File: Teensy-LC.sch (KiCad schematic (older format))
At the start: 37 parts, among them J202 Conn_01x03_Female, J203 I2C_BUS, Q201 SSM3K329R, Q202 SSM3K329R, Q203 SSM3J334R, SW201 SW_Up, SW202 SW_Down, SW203 SW_Enter, U201 LCD 2004A, U202 Teensy-LC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

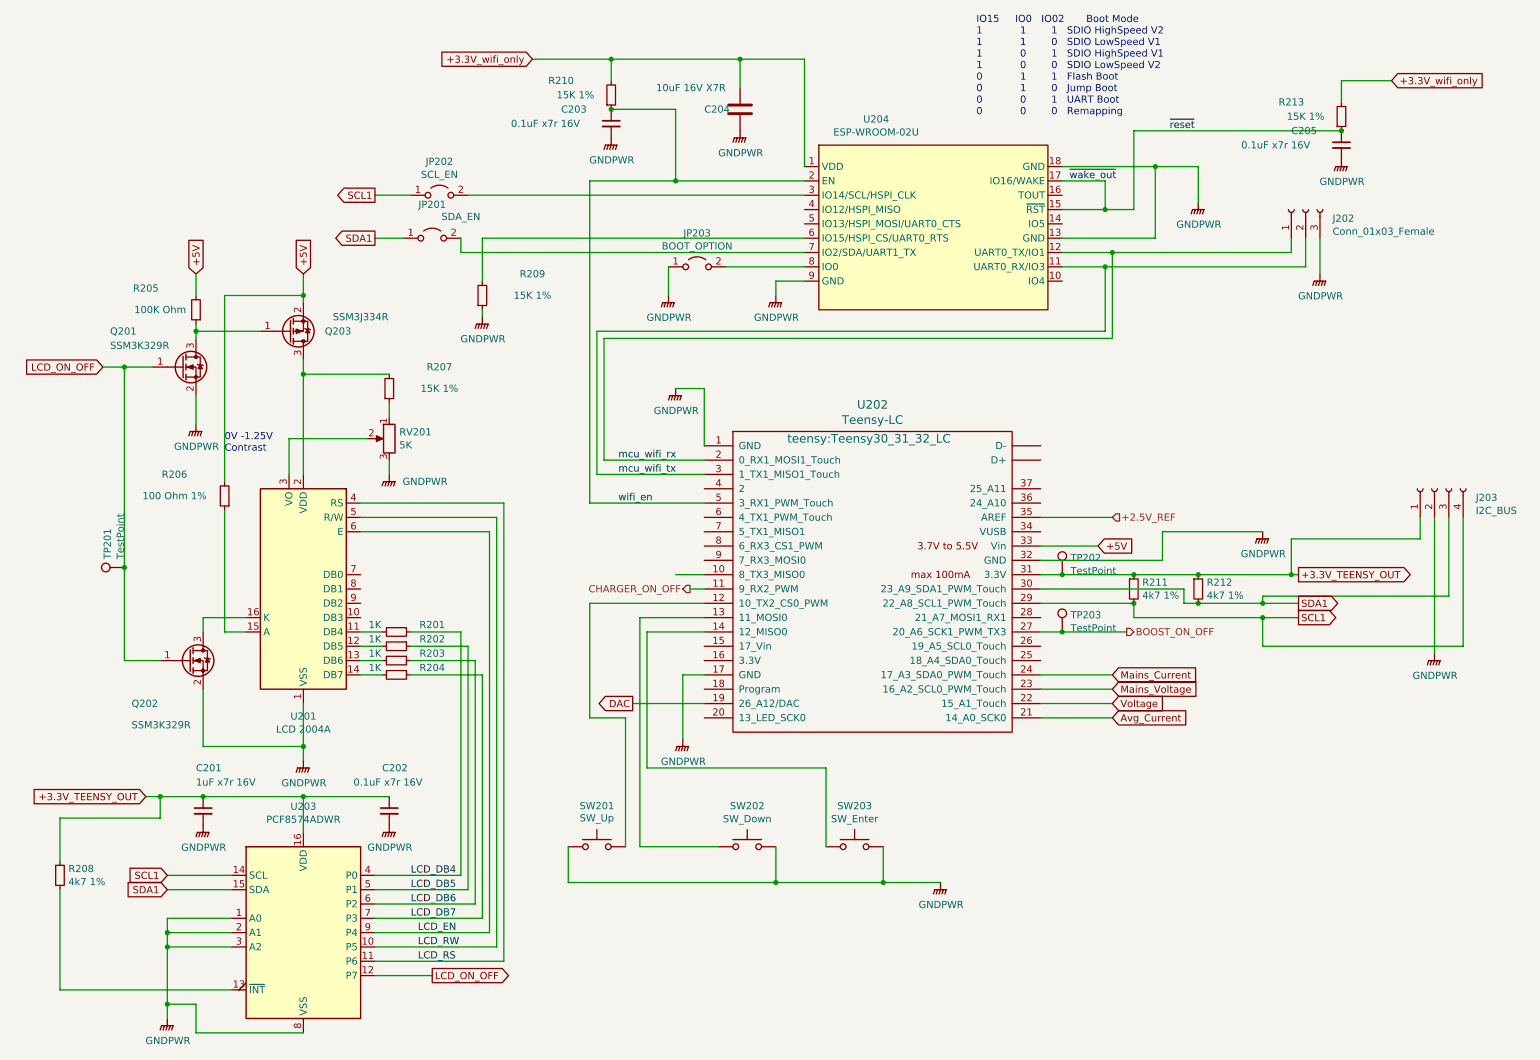
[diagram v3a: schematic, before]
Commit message: Consolidated a lot of part values that were the same part but not detected the same by Boms_away BOM editor because of subtle differences in how I specified the values. Added Digi-key part numbers to the resistors. Replaced 2mOhm .5W current sense resistors with 1W 2mOhm Thin Film resistors (lower inductance than metal element), And fixed a bug where I was earthing the return feed of the Solar inverter before passing through the current sense resistor.
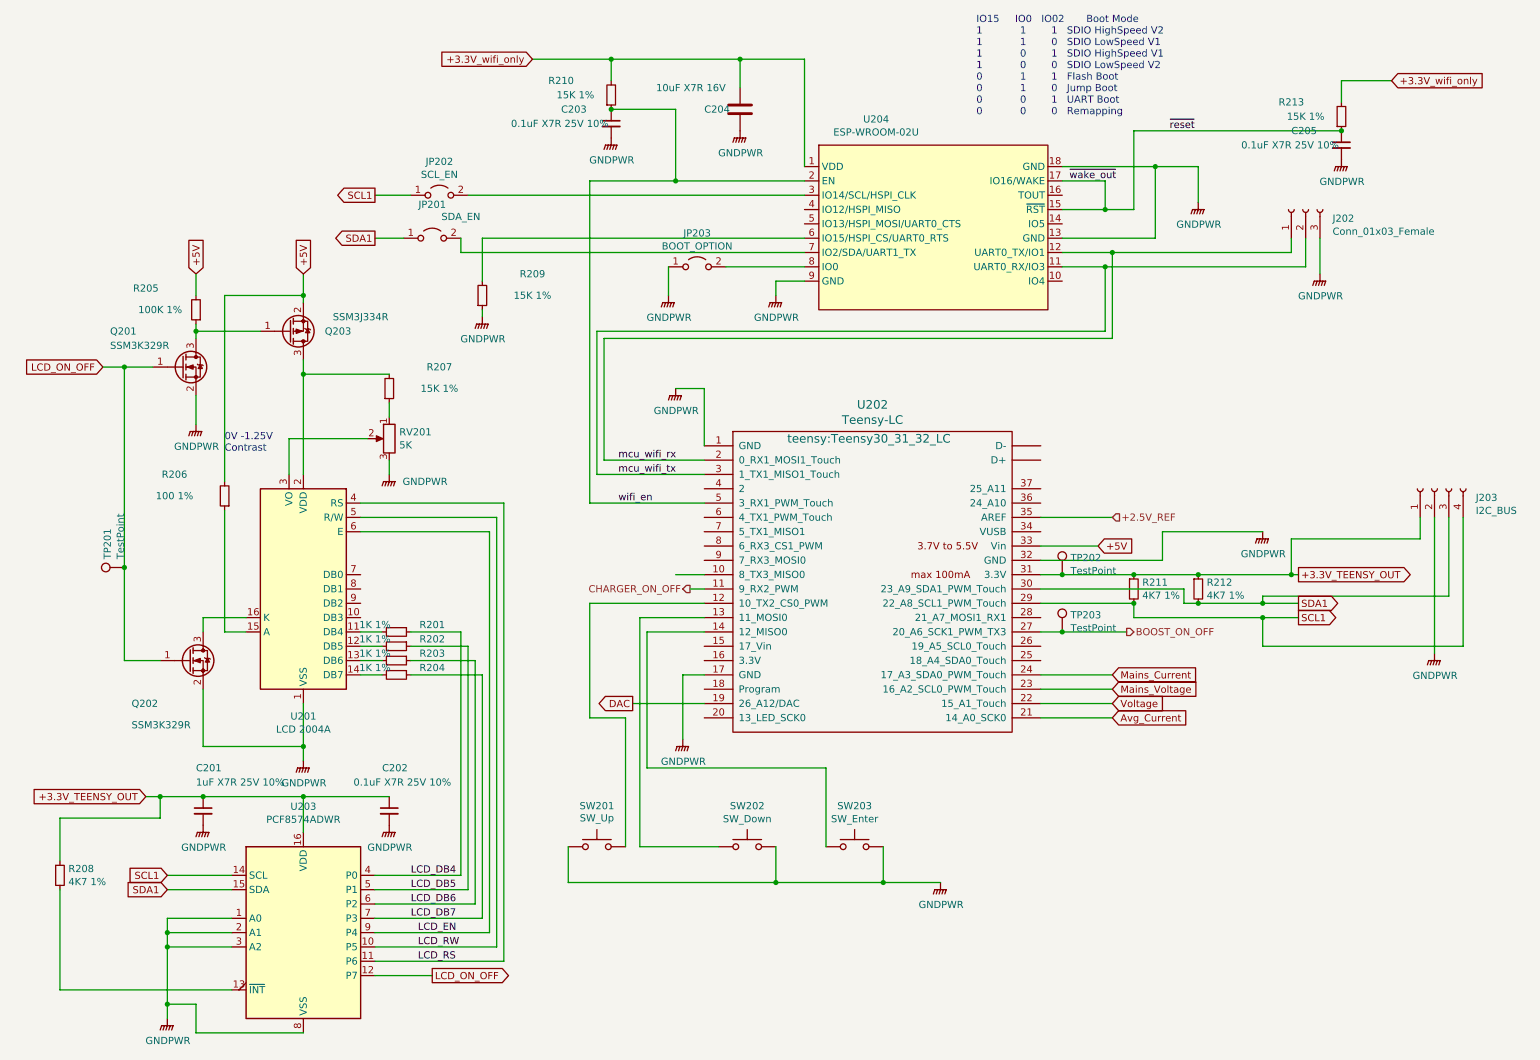
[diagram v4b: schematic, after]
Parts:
- C201: value 1uF x7r 16V -> 1uF X7R 25V 10%; MFR (none) -> Wurth Elektronik; MPN (none) -> 885012207078; SPN (none) -> 732-7672-1-ND; SPR (none) -> digikey; SPURL (none) -> -
- C202, C203, C205: value 0.1uF x7r 16V -> 0.1uF X7R 25V 10%; MFR (none) -> Samsung; MPN (none) -> CL21B104KACNNNC; SPN (none) -> 1276-1099-1-ND; SPR (none) -> digikey; SPURL (none) -> -
- C204: value 10uF 16V X7R -> 10uF X7R 16V; MFR (none) -> -; MPN (none) -> -; SPN (none) -> -; SPR (none) -> -; SPURL (none) -> -
- J202, J203, JP201, JP202, JP203, Q201, Q202, Q203, RV201, SW201, SW202, SW203, TP201, TP202, TP203, U201, U202, U203: MFR (none) -> -; MPN (none) -> -; SPN (none) -> -; SPR (none) -> -; SPURL (none) -> -
- R201, R202, R203, R204: value 1K -> 1K 1%; MFR (none) -> Yageo; MPN (none) -> RC0805FR-071KL; SPN (none) -> 311-1.00KCRCT-ND; SPR (none) -> digikey; SPURL (none) -> -
- R205: value 100K Ohm -> 100K 1%; MFR (none) -> Yageo; MPN (none) -> RC0805FR-07100KL; SPN (none) -> 311-100KCRCT-ND; SPR (none) -> digikey; SPURL (none) -> -
- R206: value 100 Ohm 1% -> 100 1%; MFR (none) -> Yageo; MPN (none) -> RC0805FR-07100RL; SPN (none) -> 311-100CRCT-ND; SPR (none) -> digikey; SPURL (none) -> -
- R207, R209, R210, R213: MFR (none) -> TE Connectivity Passive Product; MPN (none) -> CRGCQ0805F15K; SPN (none) -> A129763CT-ND; SPR (none) -> digikey; SPURL (none) -> -
- R208, R211, R212: value 4k7 1% -> 4K7 1%; MFR (none) -> -; MPN (none) -> -; SPN (none) -> -; SPR (none) -> -; SPURL (none) -> -
- U204: MFR (none) -> Espressif Systems; MPN (none) -> ESP-WROOM-02U; SPN (none) -> 1904-1022-2-ND; SPR (none) -> digikey; SPURL (none) -> -

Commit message: change a few compoents foot prints for SOT23 to SOT23-Handsoldered, and SOT23-5 to SOT23-5-Handsoldered
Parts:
- R206: value 100 1% -> 100R 1%
- R208, R211, R212: MFR - -> Yageo; MPN - -> RC0805FR-074K7L; SPN - -> 311-4.70KCRCT-ND; SPR - -> digikey
- SW201, SW202, SW203: MFR - -> TE Connectivity ALCOSWITCH Switches; MPN - -> FSM104; SPN - -> 450-1127-ND; SPR - -> digikey
- U203: MFR - -> Texas Instruments; MPN - -> PCF8574ADWR; SPN - -> 296-13105-1-ND; SPR - -> digikey

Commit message: Finished adding digi key part numbers, for now git add *
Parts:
- C204: value 10uF X7R 16V -> 10uF X7R 25V 10%; MFR - -> Samsung Electro-Mechanics; MPN - -> CL31B106KAHNNNE; SPN - -> 1276-1804-1-ND; SPR - -> digikey
- J202: MFR - -> Sullins Connector Solutions; MPN - -> PREC003SAAN-RC; SPN - -> S1012EC-03-ND; SPR - -> digikey
- J203: MFR - -> Adam Tech; MPN - -> PH1-04-UA; SPN - -> 2057-PH1-04-UA-ND; SPR - -> digikey
- JP201, JP202, JP203: MFR - -> Sullins Connector Solutions; MPN - -> PREC002SAAN-RC; SPN - -> S1012EC-02-ND; SPR - -> digikey
- Q201, Q202: MFR - -> Toshiba Semiconductor and Storage; MPN - -> SSM3K329R,LF; SPN - -> SSM3K329RLFCT-ND; SPR - -> digikey
- Q203: MFR - -> Toshiba Semiconductor and Storage; MPN - -> SSM3J334R,LF; SPN - -> SSM3J334RLFCT-ND; SPR - -> digikey
- RV201: MFR - -> Bourns Inc; MPN - -> 3006P-7-502LF; SPN - -> 3006P-7-502LF-ND; SPR - -> digikey
- U201: value LCD 2004A -> LCD 2004A Right Angle Header 16 pin 2.54mm; MFR - -> Adam Tech; MPN - -> PH1RB-16-UA; SPN - -> 2057-PH1RB-16-UA-ND; SPR - -> digikey
- U202: MFR - -> SparkFun Electronics; MPN - -> DEV-13305; SPN - -> 1568-1233-ND; SPR - -> digikey
- U204: SPN 1904-1022-2-ND -> 1904-1022-1-ND
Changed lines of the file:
@@
 F 1 "Teensy-LC" H 6375 5631 60 0000 C CNN
 F 2 "teensy:Teensy30_31_32_LC" H 6350 5500 60 0000 C CNN
-F 3 "" H 6350 3950 60 0000 C CNN
-F 4 "-" H 0 0 50 0001 C CNN "MFR"
-F 5 "-" H 0 0 50 0001 C CNN "MPN"
-F 6 "-" H 0 0 50 0001 C CNN "SPR"
-F 7 "-" H 0 0 50 0001 C CNN "SPN"
+F 3 "https://media.digikey.com/pdf/Data%20Sheets/Sparkfun%20PDFs/DEV-13305_Web.pdf" H 6350 3950 60 0001 C CNN
+F 4 "SparkFun Electronics" H 0 0 50 0001 C CNN "MFR"
+F 5 "DEV-13305" H 0 0 50 0001 C CNN "MPN"
+F 6 "digikey" H 0 0 50 0001 C CNN "SPR"
+F 7 "1568-1233-ND" H 0 0 50 0001 C CNN "SPN"
 F 8 "-" H 0 0 50 0001 C CNN "SPURL"
 	1    6350 4500
@@
 F 2 "Package_TO_SOT_SMD:SOT-23_Handsoldering" H 1750 3100 50 0001 C CNN
 F 3 "https://toshiba.semicon-storage.com/info/docget.jsp?did=2157&prodName=SSM3K329R" H 1550 3000 50 0001 C CNN
-F 4 "-" H 0 0 50 0001 C CNN "MFR"
-F 5 "-" H 0 0 50 0001 C CNN "MPN"
-F 6 "-" H 0 0 50 0001 C CNN "SPR"
-F 7 "-" H 0 0 50 0001 C CNN "SPN"
+F 4 "Toshiba Semiconductor and Storage" H 0 0 50 0001 C CNN "MFR"
+F 5 "SSM3K329R,LF" H 0 0 50 0001 C CNN "MPN"
+F 6 "digikey" H 0 0 50 0001 C CNN "SPR"
+F 7 "SSM3K329RLFCT-ND" H 0 0 50 0001 C CNN "SPN"
 F 8 "-" H 0 0 50 0001 C CNN "SPURL"
 	1    1550 3000
@@
 F 2 "Package_TO_SOT_SMD:SOT-23_Handsoldering" H 2500 2850 50 0001 C CNN
 F 3 "https://toshiba.semicon-storage.com/info/docget.jsp?did=5579&prodName=SSM3J334R" H 2300 2750 50 0001 C CNN
-F 4 "-" H 0 0 50 0001 C CNN "MFR"
-F 5 "-" H 0 0 50 0001 C CNN "MPN"
-F 6 "-" H 0 0 50 0001 C CNN "SPR"
-F 7 "-" H 0 0 50 0001 C CNN "SPN"
+F 4 "Toshiba Semiconductor and Storage" H 0 0 50 0001 C CNN "MFR"
+F 5 "SSM3J334R,LF" H 0 0 50 0001 C CNN "MPN"
+F 6 "digikey" H 0 0 50 0001 C CNN "SPR"
+F 7 "SSM3J334RLFCT-ND" H 0 0 50 0001 C CNN "SPN"
 F 8 "-" H 0 0 50 0001 C CNN "SPURL"
 	1    2300 2750
@@
 F 2 "Package_TO_SOT_SMD:SOT-23_Handsoldering" H 1800 5150 50 0001 C CNN
 F 3 "https://toshiba.semicon-storage.com/info/docget.jsp?did=2157&prodName=SSM3K329R" H 1600 5050 50 0001 C CNN
-F 4 "-" H 0 0 50 0001 C CNN "MFR"
-F 5 "-" H 0 0 50 0001 C CNN "MPN"
-F 6 "-" H 0 0 50 0001 C CNN "SPR"
-F 7 "-" H 0 0 50 0001 C CNN "SPN"
+F 4 "Toshiba Semiconductor and Storage" H 0 0 50 0001 C CNN "MFR"
+F 5 "SSM3K329R,LF" H 0 0 50 0001 C CNN "MPN"
+F 6 "digikey" H 0 0 50 0001 C CNN "SPR"
+F 7 "SSM3K329RLFCT-ND" H 0 0 50 0001 C CNN "SPN"
 F 8 "-" H 0 0 50 0001 C CNN "SPURL"
 	1    1600 5050
@@
 F 2 "Potentiometers:Potentiometer_Trimmer_Bourns_3006P" H 3000 3500 50 0001 C CNN
 F 3 "https://www.bourns.com/docs/Product-Datasheets/3306.pdf" H 3000 3500 50 0001 C CNN
-F 4 "-" H 0 0 50 0001 C CNN "MFR"
-F 5 "-" H 0 0 50 0001 C CNN "MPN"
-F 6 "-" H 0 0 50 0001 C CNN "SPR"
-F 7 "-" H 0 0 50 0001 C CNN "SPN"
+F 4 "Bourns Inc" H 0 0 50 0001 C CNN "MFR"
+F 5 "3006P-7-502LF" H 0 0 50 0001 C CNN "MPN"
+F 6 "digikey" H 0 0 50 0001 C CNN "SPR"
+F 7 "3006P-7-502LF-ND" H 0 0 50 0001 C CNN "SPN"
 F 8 "-" H 0 0 50 0001 C CNN "SPURL"
 	1    3000 3500
@@
 F 5 "ESP-WROOM-02U" H 0 0 50 0001 C CNN "MPN"
 F 6 "digikey" H 0 0 50 0001 C CNN "SPR"
-F 7 "1904-1022-2-ND" H 0 0 50 0001 C CNN "SPN"
+F 7 "1904-1022-1-ND" H 0 0 50 0001 C CNN "SPN"
 F 8 "-" H 0 0 50 0001 C CNN "SPURL"
 	1    6400 2050
@@
 AR Path="/5EF73D52/5F9FA343" Ref="C204" Part="1"
 F 0 "C204" H 5200 1200 50 0000 L CNN
-F 1 "10uF X7R 16V" H 5350 1350 50 0000 R CNN
+F 1 "10uF X7R 25V 10%" H 5350 1350 50 0000 R CNN
 F 2 "Capacitors_SMD:C_1206_HandSoldering" H 5488 1050 50 0001 C CNN
-F 3 "https://product.tdk.com/info/en/catalog/datasheets/mlcc_automotive_general_en.pdf?ref_disty=digikey" H 5450 1200 50 0001 C CNN
-F 4 "-" H 0 0 50 0001 C CNN "MFR"
-F 5 "-" H 0 0 50 0001 C CNN "MPN"
-F 6 "-" H 0 0 50 0001 C CNN "SPR"
-F 7 "-" H 0 0 50 0001 C CNN "SPN"
+F 3 "http://www.samsungsem.com/kr/support/product-search/mlcc/CL31B106KAHNNNE.jsp" H 5450 1200 50 0001 C CNN
+F 4 "Samsung Electro-Mechanics" H 0 0 50 0001 C CNN "MFR"
+F 5 "CL31B106KAHNNNE" H 0 0 50 0001 C CNN "MPN"
+F 6 "digikey" H 0 0 50 0001 C CNN "SPR"
+F 7 "1276-1804-1-ND" H 0 0 50 0001 C CNN "SPN"
 F 8 "-" H 0 0 50 0001 C CNN "SPURL"
 	1    5450 1200
@@
 F 1 "BOOT_OPTION" H 5150 2444 50 0000 C CNN
 F 2 "Pin_Headers:Pin_Header_Straight_1x02_Pitch2.54mm" H 5150 2300 50 0001 C CNN
-F 3 "~" H 5150 2300 50 0001 C CNN
-F 4 "-" H 0 0 50 0001 C CNN "MFR"
-F 5 "-" H 0 0 50 0001 C CNN "MPN"
-F 6 "-" H 0 0 50 0001 C CNN "SPR"
-F 7 "-" H 0 0 50 0001 C CNN "SPN"
+F 3 "https://media.digikey.com/PDF/Data%20Sheets/Sullins%20PDFs/z%20RzCzzzSzzN-RC,%20ST,11635-B.pdf" H 5150 2300 50 0001 C CNN
+F 4 "Sullins Connector Solutions" H 0 0 50 0001 C CNN "MFR"
+F 5 "PREC002SAAN-RC" H 0 0 50 0001 C CNN "MPN"
+F 6 "digikey" H 0 0 50 0001 C CNN "SPR"
+F 7 "S1012EC-02-ND" H 0 0 50 0001 C CNN "SPN"
 F 8 "-" H 0 0 50 0001 C CNN "SPURL"
 	1    5150 2300
@@
 F 1 "Conn_01x03_Female" V 9247 1712 50 0000 R CNN
 F 2 "Pin_Headers:Pin_Header_Straight_1x03_Pitch2.54mm" H 9400 1900 50 0001 C CNN
-F 3 "~" H 9400 1900 50 0001 C CNN
-F 4 "-" H 0 0 50 0001 C CNN "MFR"
-F 5 "-" H 0 0 50 0001 C CNN "MPN"
-F 6 "-" H 0 0 50 0001 C CNN "SPR"
-F 7 "-" H 0 0 50 0001 C CNN "SPN"
+F 3 "https://media.digikey.com/PDF/Data%20Sheets/Sullins%20PDFs/z%20RzCzzzSzzN-RC,%20ST,11635-B.pdf" H 9400 1900 50 0001 C CNN
+F 4 "Sullins Connector Solutions" H 0 0 50 0001 C CNN "MFR"
+F 5 "PREC003SAAN-RC" H 0 0 50 0001 C CNN "MPN"
+F 6 "digikey" H 0 0 50 0001 C CNN "SPR"
+F 7 "S1012EC-03-ND" H 0 0 50 0001 C CNN "SPN"
 F 8 "-" H 0 0 50 0001 C CNN "SPURL"
 	1    9400 1900
@@
 F 1 "SDA_EN" H 3500 2250 50 0000 C CNN
 F 2 "Pin_Headers:Pin_Header_Straight_1x02_Pitch2.54mm" H 3300 2100 50 0001 C CNN
-F 3 "~" H 3300 2100 50 0001 C CNN
-F 4 "-" H 0 0 50 0001 C CNN "MFR"
-F 5 "-" H 0 0 50 0001 C CNN "MPN"
-F 6 "-" H 0 0 50 0001 C CNN "SPR"
-F 7 "-" H 0 0 50 0001 C CNN "SPN"
+F 3 "https://media.digikey.com/PDF/Data%20Sheets/Sullins%20PDFs/z%20RzCzzzSzzN-RC,%20ST,11635-B.pdf" H 3300 2100 50 0001 C CNN
+F 4 "Sullins Connector Solutions" H 0 0 50 0001 C CNN "MFR"
+F 5 "PREC002SAAN-RC" H 0 0 50 0001 C CNN "MPN"
+F 6 "digikey" H 0 0 50 0001 C CNN "SPR"
+F 7 "S1012EC-02-ND" H 0 0 50 0001 C CNN "SPN"
 F 8 "-" H 0 0 50 0001 C CNN "SPURL"
 	1    3300 2100
@@
 F 1 "SCL_EN" H 3350 1944 50 0000 C CNN
 F 2 "Pin_Headers:Pin_Header_Straight_1x02_Pitch2.54mm" H 3350 1800 50 0001 C CNN
-F 3 "~" H 3350 1800 50 0001 C CNN
-F 4 "-" H 0 0 50 0001 C CNN "MFR"
-F 5 "-" H 0 0 50 0001 C CNN "MPN"
-F 6 "-" H 0 0 50 0001 C CNN "SPR"
-F 7 "-" H 0 0 50 0001 C CNN "SPN"
+F 3 "https://media.digikey.com/PDF/Data%20Sheets/Sullins%20PDFs/z%20RzCzzzSzzN-RC,%20ST,11635-B.pdf" H 3350 1800 50 0001 C CNN
+F 4 "Sullins Connector Solutions" H 0 0 50 0001 C CNN "MFR"
+F 5 "PREC002SAAN-RC" H 0 0 50 0001 C CNN "MPN"
+F 6 "digikey" H 0 0 50 0001 C CNN "SPR"
+F 7 "S1012EC-02-ND" H 0 0 50 0001 C CNN "SPN"
 F 8 "-" H 0 0 50 0001 C CNN "SPURL"
 	1    3350 1800
@@
 F 1 "I2C_BUS" V 10147 3562 50 0000 R CNN
 F 2 "Pin_Headers:Pin_Header_Straight_1x04_Pitch2.54mm" H 10300 3850 50 0001 C CNN
-F 3 "~" H 10300 3850 50 0001 C CNN
-F 4 "-" H 0 0 50 0001 C CNN "MFR"
-F 5 "-" H 0 0 50 0001 C CNN "MPN"
-F 6 "-" H 0 0 50 0001 C CNN "SPR"
-F 7 "-" H 0 0 50 0001 C CNN "SPN"
+F 3 "http://www.adam-tech.com/downloader.php?p=PH1-XX-UA.pdf" H 10300 3850 50 0001 C CNN
+F 4 "Adam Tech" H 0 0 50 0001 C CNN "MFR"
+F 5 "PH1-04-UA" H 0 0 50 0001 C CNN "MPN"
+F 6 "digikey" H 0 0 50 0001 C CNN "SPR"
+F 7 "2057-PH1-04-UA-ND" H 0 0 50 0001 C CNN "SPN"
 F 8 "-" H 0 0 50 0001 C CNN "SPURL"
 	1    10300 3850
@@
 P 2400 4550
 F 0 "U201" H 2400 3661 50 0000 C CNN
-F 1 "LCD 2004A" H 2400 3570 50 0000 C CNN
+F 1 "LCD 2004A Right Angle Header 16 pin 2.54mm" H 2400 3570 50 0000 C CNN
 F 2 "Connect_jl:LCD2004_Pin_Header_Angled_1x16_Pitch2.54mm" H 2400 3650 50 0001 C CNN
 F 3 "/media/jlynch/SW_Preload/Users/jlynch/Downloads/DataSheets/LCD/2004A-RK-10290_410.pdf" H 2500 4450 50 0001 C CNN
 F 4 "http://www.adam-tech.com/downloader.php?p=PH1RB-XX-UA.pdf" H 2400 4550 50 0001 C CNN "Connector"
-F 5 "-" H 0 0 50 0001 C CNN "MFR"
-F 6 "-" H 0 0 50 0001 C CNN "MPN"
-F 7 "-" H 0 0 50 0001 C CNN "SPR"
-F 8 "-" H 0 0 50 0001 C CNN "SPN"
+F 5 "Adam Tech" H 0 0 50 0001 C CNN "MFR"
+F 6 "PH1RB-16-UA" H 0 0 50 0001 C CNN "MPN"
+F 7 "digikey" H 0 0 50 0001 C CNN "SPR"
+F 8 "2057-PH1RB-16-UA-ND" H 0 0 50 0001 C CNN "SPN"
 F 9 "-" H 0 0 50 0001 C CNN "SPURL"
 	1    2400 4550
